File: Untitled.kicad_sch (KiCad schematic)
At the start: 20 parts, among them J1 Battery Connector, J2 Pyro Ignition Terminal, J3 Pyro Voltage Terminal, Q1 Q_NMOS_DGS, Q2 Q_NMOS_DGS, Q3 Q_NMOS_DGS, U1 XIAO-ESP32-S3-SMD, U3 LSM6DSO32, U4 MS5611-01BA

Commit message: Experimental Layout
Changed screw terminal footprint to accurately reflect existing club stock of smaller terminals (2.54mm pitch thru-hole). Experimented with trying to make a single board layout work for the flight computer.
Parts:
- C1, C2, C3: footprint Capacitor_SMD:C_0805_2012Metric_Pad1.18x1.45mm_HandSolder -> Capacitor_SMD:C_0805_2012Metric
- J2, J3: footprint TerminalBlock_Phoenix:TerminalBlock_Phoenix_MKDS-1,5-3-5.08_1x03_P5.08mm_Horizontal -> TerminalBlock_Phoenix:TerminalBlock_Phoenix_MPT-0,5-3-2.54_1x03_P2.54mm_Horizontal
- R1, R2, R3, R4, R5, R6, R7, R8: footprint Resistor_SMD:R_0805_2012Metric_Pad1.20x1.40mm_HandSolder -> Resistor_SMD:R_0805_2012Metric
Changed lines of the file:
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@@
 			)
 		)
-		(property "Footprint" "TerminalBlock_Phoenix:TerminalBlock_Phoenix_MKDS-1,5-3-5.08_1x03_P5.08mm_Horizontal"
+		(property "Footprint" "TerminalBlock_Phoenix:TerminalBlock_Phoenix_MPT-0,5-3-2.54_1x03_P2.54mm_Horizontal"
 			(at 208.28 71.12 0)
 			(effects
@@
 			)
 		)
-		(property "Footprint" "Resistor_SMD:R_0805_2012Metric_Pad1.20x1.40mm_HandSolder"
+		(property "Footprint" "Resistor_SMD:R_0805_2012Metric"
 			(at 51.816 94.996 90)
 			(effects
@@
 			)
 		)
-		(property "Footprint" "Resistor_SMD:R_0805_2012Metric_Pad1.20x1.40mm_HandSolder"
+		(property "Footprint" "Resistor_SMD:R_0805_2012Metric"
 			(at 51.816 145.796 90)
 			(effects
@@
 			)
 		)
-		(property "Footprint" "Resistor_SMD:R_0805_2012Metric_Pad1.20x1.40mm_HandSolder"
+		(property "Footprint" "Resistor_SMD:R_0805_2012Metric"
 			(at 51.816 110.236 90)
 			(effects
@@
 			)
 		)
-		(property "Footprint" "Resistor_SMD:R_0805_2012Metric_Pad1.20x1.40mm_HandSolder"
+		(property "Footprint" "Resistor_SMD:R_0805_2012Metric"
 			(at 51.816 166.116 90)
 			(effects
@@
 			)
 		)
-		(property "Footprint" "TerminalBlock_Phoenix:TerminalBlock_Phoenix_MKDS-1,5-3-5.08_1x03_P5.08mm_Horizontal"
+		(property "Footprint" "TerminalBlock_Phoenix:TerminalBlock_Phoenix_MPT-0,5-3-2.54_1x03_P2.54mm_Horizontal"
 			(at 208.28 91.44 0)
 			(effects
@@
 			)
 		)
-		(property "Footprint" "Resistor_SMD:R_0805_2012Metric_Pad1.20x1.40mm_HandSolder"
+		(property "Footprint" "Resistor_SMD:R_0805_2012Metric"
 			(at 107.696 150.114 90)
 			(effects
@@
 			)
 		)
-		(property "Footprint" "Resistor_SMD:R_0805_2012Metric_Pad1.20x1.40mm_HandSolder"
+		(property "Footprint" "Resistor_SMD:R_0805_2012Metric"
 			(at 51.816 130.556 90)
 			(effects
@@
 			)
 		)
-		(property "Footprint" "Capacitor_SMD:C_0805_2012Metric_Pad1.18x1.45mm_HandSolder"
+		(property "Footprint" "Capacitor_SMD:C_0805_2012Metric"
 			(at 257.81 144.78 0)
 			(effects
@@
 			)
 		)
-		(property "Footprint" "Capacitor_SMD:C_0805_2012Metric_Pad1.18x1.45mm_HandSolder"
+		(property "Footprint" "Capacitor_SMD:C_0805_2012Metric"
 			(at 265.43 67.31 0)
 			(effects
@@
 			)
 		)
-		(property "Footprint" "Capacitor_SMD:C_0805_2012Metric_Pad1.18x1.45mm_HandSolder"
+		(property "Footprint" "Capacitor_SMD:C_0805_2012Metric"
 			(at 269.24 144.78 0)
 			(effects
@@
 			)
 		)
-		(property "Footprint" "Resistor_SMD:R_0805_2012Metric_Pad1.20x1.40mm_HandSolder"
+		(property "Footprint" "Resistor_SMD:R_0805_2012Metric"
 			(at 51.816 181.356 90)
 			(effects
@@
 			)
 		)
-		(property "Footprint" "Resistor_SMD:R_0805_2012Metric_Pad1.20x1.40mm_HandSolder"
+		(property "Footprint" "Resistor_SMD:R_0805_2012Metric"
 			(at 117.856 150.114 90)
 			(effects

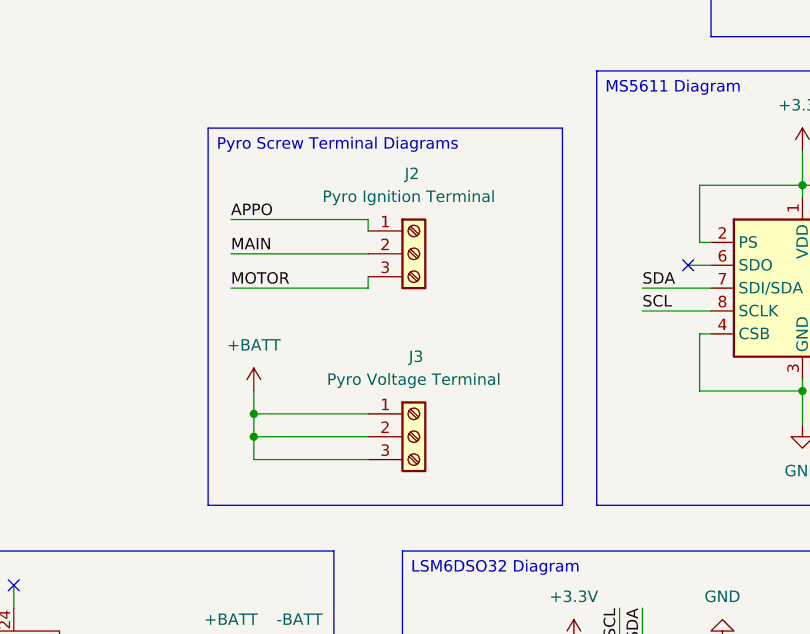
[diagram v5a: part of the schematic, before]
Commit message: Basic Schematic (NO PCB DESIGN DONE)
Removed any PCB design so people can fork off and do their own PCB designs.
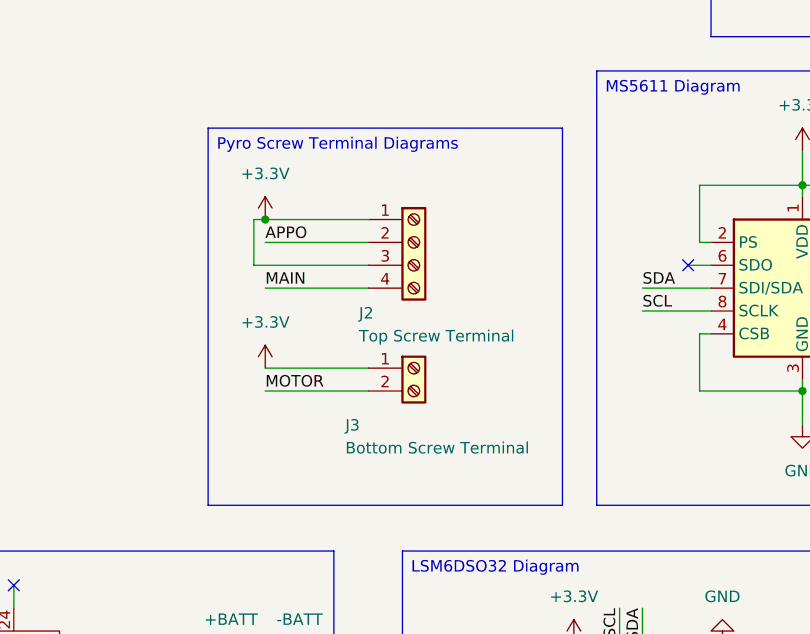
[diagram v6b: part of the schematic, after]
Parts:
- removed J2: Pyro Ignition Terminal, TerminalBlock_Phoenix:TerminalBlock_Phoenix_MPT-0,5-3-2.54_1x03_P2.54mm_Horizontal, symbol Connector:Screw_Terminal_01x03
- removed J3: Pyro Voltage Terminal, TerminalBlock_Phoenix:TerminalBlock_Phoenix_MPT-0,5-3-2.54_1x03_P2.54mm_Horizontal, symbol Connector:Screw_Terminal_01x03
- added J2: Top Screw Terminal, TerminalBlock_Phoenix:TerminalBlock_Phoenix_MPT-0,5-4-2.54_1x04_P2.54mm_Horizontal, symbol Connector:Screw_Terminal_01x04
- added J3: Bottom Screw Terminal, TerminalBlock_Phoenix:TerminalBlock_Phoenix_MPT-0,5-2-2.54_1x02_P2.54mm_Horizontal, symbol Connector:Screw_Terminal_01x02
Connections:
- net +3.3V: now also J2.1 (Pin_1), J2.3 (Pin_3), J3.1 (Pin_1)
- net APPO: now also J2.2 (Pin_2)
- net MAIN: now also J2.4 (Pin_4)
- net MOTOR: now also J3.2 (Pin_2)

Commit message: Initial Layout
Did some work on the initial versions of my PCB layout
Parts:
- C1, C2, C3: footprint Capacitor_SMD:C_0805_2012Metric -> Capacitor_SMD:C_0603_1608Metric
- R1, R2, R3, R4, R5, R6, R7, R8: footprint Resistor_SMD:R_0805_2012Metric -> Resistor_SMD:R_0402_1005Metric
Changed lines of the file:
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@@
 			)
 		)
-		(property "Footprint" "Resistor_SMD:R_0805_2012Metric"
+		(property "Footprint" "Resistor_SMD:R_0402_1005Metric"
 			(at 51.816 94.996 90)
 			(effects
@@
 			)
 		)
-		(property "Footprint" "Resistor_SMD:R_0805_2012Metric"
+		(property "Footprint" "Resistor_SMD:R_0402_1005Metric"
 			(at 51.816 145.796 90)
 			(effects
@@
 			)
 		)
-		(property "Footprint" "Resistor_SMD:R_0805_2012Metric"
+		(property "Footprint" "Resistor_SMD:R_0402_1005Metric"
 			(at 51.816 110.236 90)
 			(effects
@@
 			)
 		)
-		(property "Footprint" "Resistor_SMD:R_0805_2012Metric"
+		(property "Footprint" "Resistor_SMD:R_0402_1005Metric"
 			(at 51.816 166.116 90)
 			(effects
@@
 			)
 		)
-		(property "Footprint" "Resistor_SMD:R_0805_2012Metric"
+		(property "Footprint" "Resistor_SMD:R_0402_1005Metric"
 			(at 107.696 150.114 90)
 			(effects
@@
 			)
 		)
-		(property "Footprint" "Resistor_SMD:R_0805_2012Metric"
+		(property "Footprint" "Resistor_SMD:R_0402_1005Metric"
 			(at 51.816 130.556 90)
 			(effects
@@
 			)
 		)
-		(property "Footprint" "Capacitor_SMD:C_0805_2012Metric"
+		(property "Footprint" "Capacitor_SMD:C_0603_1608Metric"
 			(at 257.81 144.78 0)
 			(effects
@@
 			)
 		)
-		(property "Footprint" "Capacitor_SMD:C_0805_2012Metric"
+		(property "Footprint" "Capacitor_SMD:C_0603_1608Metric"
 			(at 265.43 67.31 0)
 			(effects
@@
 			)
 		)
-		(property "Footprint" "Capacitor_SMD:C_0805_2012Metric"
+		(property "Footprint" "Capacitor_SMD:C_0603_1608Metric"
 			(at 269.24 144.78 0)
 			(effects
@@
 			)
 		)
-		(property "Footprint" "Resistor_SMD:R_0805_2012Metric"
+		(property "Footprint" "Resistor_SMD:R_0402_1005Metric"
 			(at 51.816 181.356 90)
 			(effects
@@
 			)
 		)
-		(property "Footprint" "Resistor_SMD:R_0805_2012Metric"
+		(property "Footprint" "Resistor_SMD:R_0402_1005Metric"
 			(at 117.856 150.114 90)
 			(effects
